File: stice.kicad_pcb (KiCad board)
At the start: 2 copper layers, 74 parts, among them SW1 SW_Push, SW10 SW_Push, SW11 SW_Push, SW12 SW_Push, SW13 SW_Push, SW14 SW_Push, SW15 SW_Push, SW16 SW_Push, SW17 SW_Push, SW18 SW_Push, SW19 SW_Push, SW2 SW_Push, SW20 SW_Push, SW21 SW_Push, SW22 SW_Push, SW23 SW_Push, SW24 SW_Push, SW25 SW_Push, SW26 SW_Push, SW27 SW_Push, SW28 SW_Push, SW29 SW_Push, SW3 SW_Push, SW30 SW_Push, SW31 SW_Push, SW32 SW_Push, SW33 SW_Push, SW34 SW_Push, SW35 SW_Push, SW36 SW_Push, SW37 SW_Push, SW4 SW_Push, SW5 SW_Push, SW6 SW_Push, SW7 SW_Push, SW8 SW_Push, SW9 SW_Push, U1 nice_nano

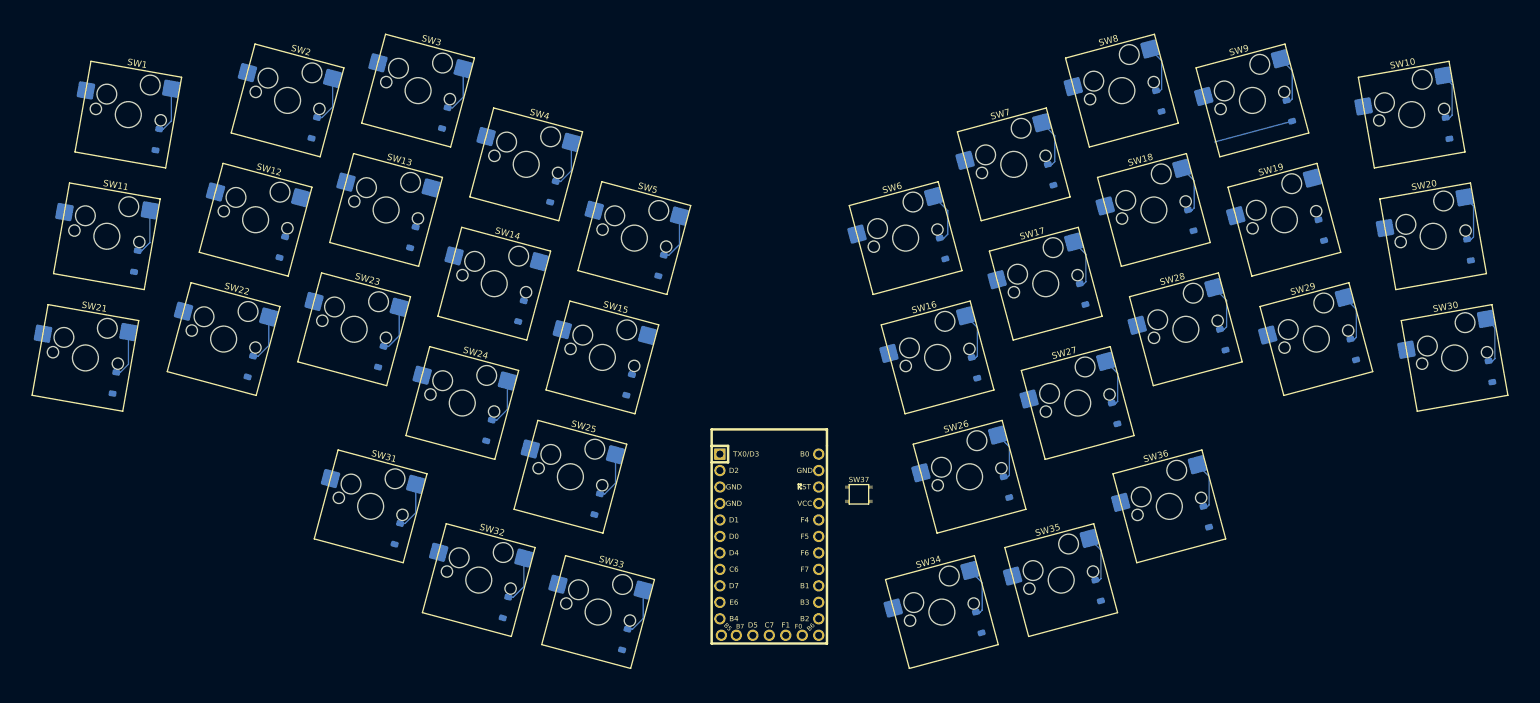
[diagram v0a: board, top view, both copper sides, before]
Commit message: outline done
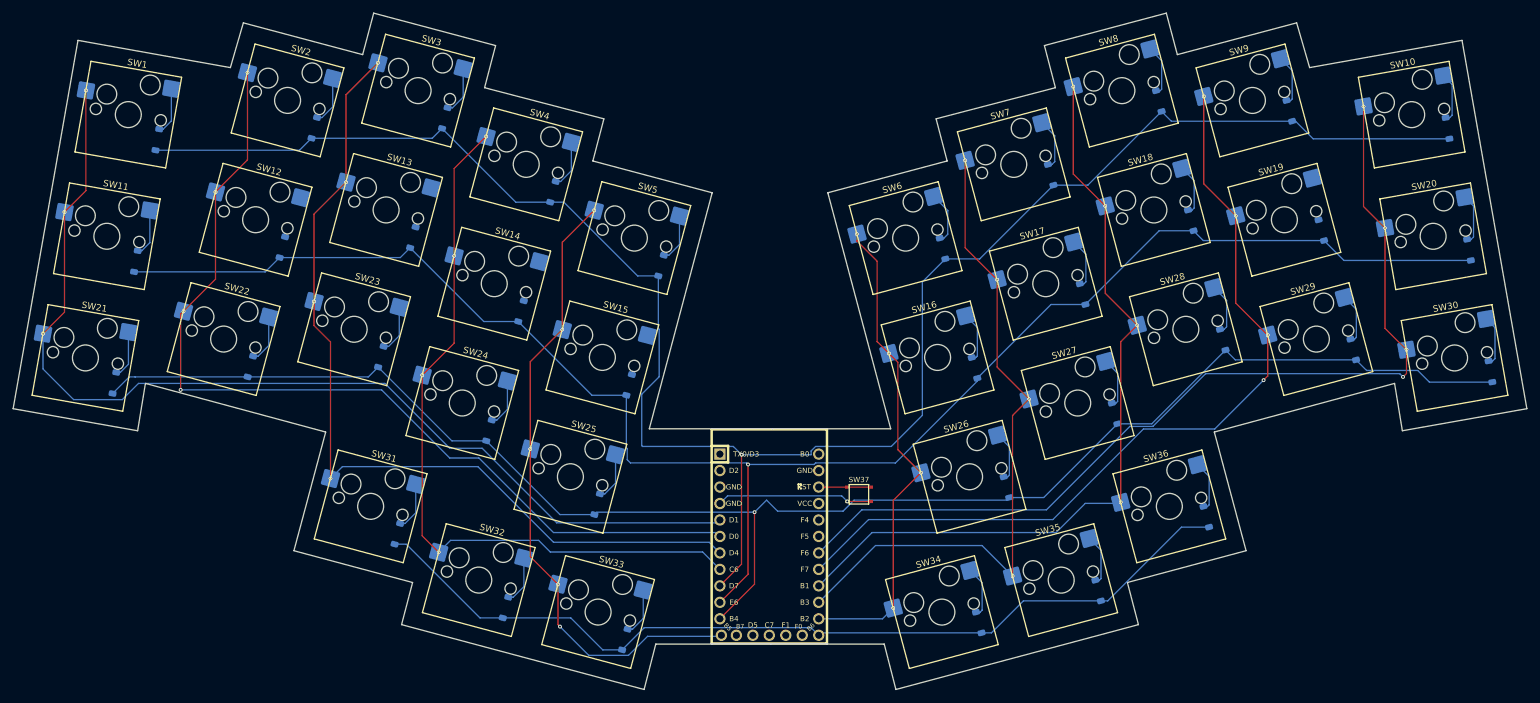
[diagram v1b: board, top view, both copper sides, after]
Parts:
- renumbered D34 to D10, D2 to D11, D9 to D12, D8 to D13, D10 to D14, D11 to D15, D26 to D16, D24 to D17, D23 to D18, D25 to D19, D5 to D2, D35 to D20, D3 to D21, D13 to D22, D12 to D23, D14 to D24, D15 to D25, D30 to D26, D28 to D27, D27 to D28, D4 to D3, D36 to D30, D16 to D31, D17 to D32, D18 to D33, D32 to D34, D33 to D35, D31 to D36, D6 to D4, D7 to D5, D22 to D6, D20 to D7, D19 to D8, D21 to D9
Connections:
- D10 pad 1: ROW3 -> ROW0
- D10 pad 2: Net-(D34-A) -> Net-(D10-A)
- D11 pad 1: ROW0 -> ROW1
- D11 pad 2: Net-(D2-A) -> Net-(D11-A)
- D12 pad 1: ROW0 -> ROW1
- D12 pad 2: Net-(D9-A) -> Net-(D12-A)
- D13 pad 1: ROW0 -> ROW1
- D13 pad 2: Net-(D8-A) -> Net-(D13-A)
- D14 pad 1: ROW0 -> ROW1
- D14 pad 2: Net-(D10-A) -> Net-(D14-A)
- D15 pad 2: Net-(D11-A) -> Net-(D15-A)
- D16 pad 1: ROW2 -> ROW1
- D16 pad 2: Net-(D26-A) -> Net-(D16-A)
- D17 pad 1: ROW2 -> ROW1
- D17 pad 2: Net-(D24-A) -> Net-(D17-A)
- D18 pad 1: ROW2 -> ROW1
- D18 pad 2: Net-(D23-A) -> Net-(D18-A)
- D19 pad 1: ROW2 -> ROW1
- D19 pad 2: Net-(D25-A) -> Net-(D19-A)
- D2 pad 2: Net-(D5-A) -> Net-(D2-A)
- D20 pad 1: ROW3 -> ROW1
- D20 pad 2: Net-(D35-A) -> Net-(D20-A)
- D21 pad 1: ROW0 -> ROW2
- D21 pad 2: Net-(D3-A) -> Net-(D21-A)
- D22 pad 1: ROW1 -> ROW2
- D22 pad 2: Net-(D13-A) -> Net-(D22-A)
- D23 pad 1: ROW1 -> ROW2
- D23 pad 2: Net-(D12-A) -> Net-(D23-A)
- D24 pad 1: ROW1 -> ROW2
- D24 pad 2: Net-(D14-A) -> Net-(D24-A)
- D25 pad 1: ROW1 -> ROW2
- D25 pad 2: Net-(D15-A) -> Net-(D25-A)
- D26 pad 2: Net-(D30-A) -> Net-(D26-A)
- D27 pad 2: Net-(D28-A) -> Net-(D27-A)
- D28 pad 2: Net-(D27-A) -> Net-(D28-A)
- D3 pad 2: Net-(D4-A) -> Net-(D3-A)
- D30 pad 1: ROW3 -> ROW2
- D30 pad 2: Net-(D36-A) -> Net-(D30-A)
- D31 pad 1: ROW1 -> ROW3
- D31 pad 2: Net-(D16-A) -> Net-(D31-A)
- D32 pad 1: ROW1 -> ROW3
- D32 pad 2: Net-(D17-A) -> Net-(D32-A)
- D33 pad 1: ROW1 -> ROW3
- D33 pad 2: Net-(D18-A) -> Net-(D33-A)
- D34 pad 2: Net-(D32-A) -> Net-(D34-A)
- D35 pad 2: Net-(D33-A) -> Net-(D35-A)
- D36 pad 2: Net-(D31-A) -> Net-(D36-A)
- D4 pad 2: Net-(D6-A) -> Net-(D4-A)
- D5 pad 2: Net-(D7-A) -> Net-(D5-A)
- D6 pad 1: ROW2 -> ROW0
- D6 pad 2: Net-(D22-A) -> Net-(D6-A)
- D7 pad 1: ROW1 -> ROW0
- D7 pad 2: Net-(D20-A) -> Net-(D7-A)
- D8 pad 1: ROW1 -> ROW0
- D8 pad 2: Net-(D19-A) -> Net-(D8-A)
- D9 pad 1: ROW2 -> ROW0
- D9 pad 2: Net-(D21-A) -> Net-(D9-A)
- U1 pad 12: ROW3 -> COL4
- U1 pad 13: COL5 -> ROW3
- U1 pad 14: COL4 -> COL5
- U1 pad 15: COL3 -> COL6
- U1 pad 16: COL2 -> COL7
- U1 pad 17: COL1 -> COL8
- U1 pad 18: COL0 -> COL9
- U1 pad 3: Net-(U1-GND-Pad3) -> GND
- U1 pad 4: Net-(U1-GND-Pad3) -> GND
- U1 pad 5: COL9 -> COL0
- U1 pad 6: COL8 -> COL1
- U1 pad 7: COL7 -> COL2
- U1 pad 8: COL6 -> COL3
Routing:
- net ROW0: track 0.00 -> 298.5 mm, vias 0 -> 1
- net ROW1: track 0.00 -> 267.4 mm, vias 0 -> 1
- net ROW2: track 12.4 -> 256.5 mm, vias 0 -> 1
- net COL0: track 0.00 -> 162.2 mm, vias 0 -> 3
- net COL9: track 0.00 -> 146.4 mm, vias 0 -> 4
- net COL1: track 0.00 -> 145.7 mm, vias 0 -> 4
- net ROW3: track 0.00 -> 141.2 mm
- net COL2: track 0.00 -> 135.6 mm, vias 0 -> 4
- net COL8: track 0.00 -> 128.8 mm, vias 0 -> 4
- net COL7: track 0.00 -> 121.1 mm, vias 0 -> 4
- net COL3: track 0.00 -> 115.2 mm, vias 0 -> 4
- net COL6: track 0.00 -> 104.7 mm, vias 0 -> 4
- net COL4: track 0.00 -> 98.0 mm, vias 0 -> 5
- net COL5: track 0.00 -> 75.7 mm, vias 0 -> 4
- net GND: track 0.00 -> 24.1 mm, vias 0 -> 1
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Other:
- board outline added: 233.4 x 104.3 mm
